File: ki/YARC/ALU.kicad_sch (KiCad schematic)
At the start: 0 parts

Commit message: Major changes to ALU, Flags, and add new ALU controls schematic
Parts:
- added U? (x3): AS6C6264, symbol pdxjjb:AS6C6264
- added U? (x2): 74LS245, symbol 74xx:74LS245
- added U? (x2): 74LS574, symbol 74xx:74LS574
- added U?: 74LS573, symbol 74xx:74LS573
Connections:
- new net A0: U?.10 (A0)
- new net A1: U?.9 (A1)
- new net A2: U?.8 (A2)
- new net A3: U?.7 (A3)
- new net A4: U?.10 (A0), U?.10 (A0)
- new net A5: U?.9 (A1), U?.9 (A1)
- new net A6: U?.8 (A2), U?.8 (A2)
- new net A7: U?.7 (A3), U?.7 (A3)
- new net ALUOUT0: U?.19 (Q0)
- new net ALUOUT15: U?.12 (Q7)
- new net ALUOUT7: U?.12 (Q7)
- new net ALUOUT8: U?.19 (Q0)
- new net ALU_D0: U?.11 (DQ0), U?.2 (A0), U?.2 (D0), U?.2 (D0)
- new net ALU_D1: U?.12 (DQ1), U?.3 (A1)
- new net ALU_D2: U?.13 (DQ2), U?.4 (A2)
- new net ALU_D3: U?.15 (DQ3), U?.5 (A3)
- new net ALU_D4: U?.11 (DQ0), U?.11 (DQ0), U?.2 (A0)
- new net ALU_D5: U?.12 (DQ1), U?.12 (DQ1), U?.3 (A1)
- new net ALU_D6: U?.13 (DQ2), U?.13 (DQ2), U?.4 (A2)
- new net ALU_D7: U?.15 (DQ3), U?.15 (DQ3), U?.5 (A3), U?.9 (D7), U?.9 (D7)
- new net B0: U?.6 (A4)
- new net B1: U?.5 (A5)
- new net B2: U?.4 (A6)
- new net B3: U?.3 (A7)
- new net B4: U?.6 (A4), U?.6 (A4)
- new net B5: U?.5 (A5), U?.5 (A5)
- new net B6: U?.4 (A6), U?.4 (A6)
- new net B7: U?.3 (A7), U?.3 (A7)
- new net CARRY_IN: U?.25 (A8)
- new net DN4: U?.16 (DQ4), U?.6 (A4)
- new net DN5: U?.17 (DQ5), U?.7 (A5)
- new net DN6: U?.18 (DQ6), U?.8 (A6)
- new net DN7: U?.19 (DQ7), U?.9 (A7)
- new net F0: U?.16 (DQ4), U?.16 (DQ4), U?.6 (A4)
- new net F1: U?.17 (DQ5), U?.17 (DQ5), U?.7 (A5)
- new net F2: U?.18 (DQ6), U?.18 (DQ6), U?.8 (A6)
- new net F3: U?.19 (DQ7), U?.19 (DQ7), U?.9 (A7)
- new net FMUX0: U?.2 (D0)
- new net FMUX1: U?.3 (D1)
- new net FMUX2: U?.4 (D2)
- new net FMUX3: U?.5 (D3)
- new net GND: U?.1 (OE), U?.1 (OE), U?.10 (GND), U?.10 (GND), U?.10 (GND), U?.10 (GND), U?.10 (GND), U?.14 (GND), U?.14 (GND), U?.14 (GND), U?.6 (D4), U?.7 (D5), U?.8 (D6), U?.9 (D7)
- new net HALF_CARRY_IN: U?.25 (A8), U?.25 (A8)
- new net IRH0: U?.24 (A9), U?.24 (A9), U?.24 (A9)
- new net IRH1: U?.21 (A10), U?.21 (A10), U?.21 (A10)
- new net IRH2: U?.23 (A11), U?.23 (A11), U?.23 (A11)
- new net IRH3: U?.2 (A12), U?.2 (A12), U?.2 (A12)
- new net KX0: U?.18 (B0), U?.18 (B0)
- new net KX7: U?.11 (B7), U?.11 (B7)
- new net LONG_SYMBOL: U?.1 (OE), U?.11 (Cp), U?.19 (CE), U?.20 (CE#)
- new net REG_F0: U?.19 (Q0)
- new net REG_F1: U?.18 (Q1)
- new net REG_F2: U?.17 (Q2)
- new net REG_F3: U?.16 (Q3)
- new net VCC: U?.20 (VCC), U?.20 (VCC), U?.20 (VCC), U?.20 (VCC), U?.20 (VCC), U?.28 (Vcc), U?.28 (Vcc), U?.28 (Vcc)
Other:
- note added: "C Z N V"
- note added: "HC HZ HN HV"
- note added: "V N Z C"

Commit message: Believable ALU/Flags design almost complete
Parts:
- removed U?: 74LS574, symbol 74xx:74LS574
- gave numbers to parts that had none: 7
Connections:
- net GND: now also U116.20 (CE#), U117.20 (CE#), U117.25 (A8), U118.20 (CE#), U118.22 (OE#); no longer U122.1 (OE)
- net LONG_SYMBOL: no longer U116.20 (CE#)
- net VCC: now also U116.25 (A8), U116.26 (CE2), U117.26 (CE2), U118.26 (CE2)
- net ~{FQTR_NOT_C}: now reaches U117.22 (OE#)
- net ~{ALU_WR}: now reaches U117.27 (WE#)
- net ~{ALU_WR}: now also U116.27 (WE#), U118.27 (WE#)
- net ~{FQTR_C}: now reaches U116.22 (OE#)
- net F0 renamed FHALF.C
- net F1 renamed FHALF.Z
- net F2 renamed FHALF.N
- net F3 renamed FHALF.V
- removed net HALF_CARRY_IN: U116.25 (A8), U117.25 (A8)
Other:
- note added: "FMUXIN_Z SHEET 17"
- note removed: "C Z N V"
- note removed: "HC HZ HN HV"
- note removed: "V N Z C"

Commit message: Further development of ALU controls
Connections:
- net GND: now also U122.1 (OE); no longer U117.25 (A8), U118.22 (OE#)
- net VCC: no longer U116.25 (A8), U116.26 (CE2), U117.26 (CE2)
- net SYSADDR15: now reaches U120.1 (A->B)
- net SYSADDR15: now also U119.1 (A->B)
- net ACR3: now reaches U120.19 (CE)
- net PHI_1_CLK: now reaches U121.11 (Load)
- net LONG_SYMBOL renamed ACR2
- net ACR2: no longer U122.11 (Cp)
- net ~{ALU_WR} renamed ACR7
- new net ACR4: U116.25 (A8)
- new net ACR5: U117.25 (A8)
- new net ACR6: U118.22 (OE#)
- new net PHI_2_CLK: U122.11 (Cp)
- new net ~{ACR_ERR}: U116.26 (CE2), U117.26 (CE2)

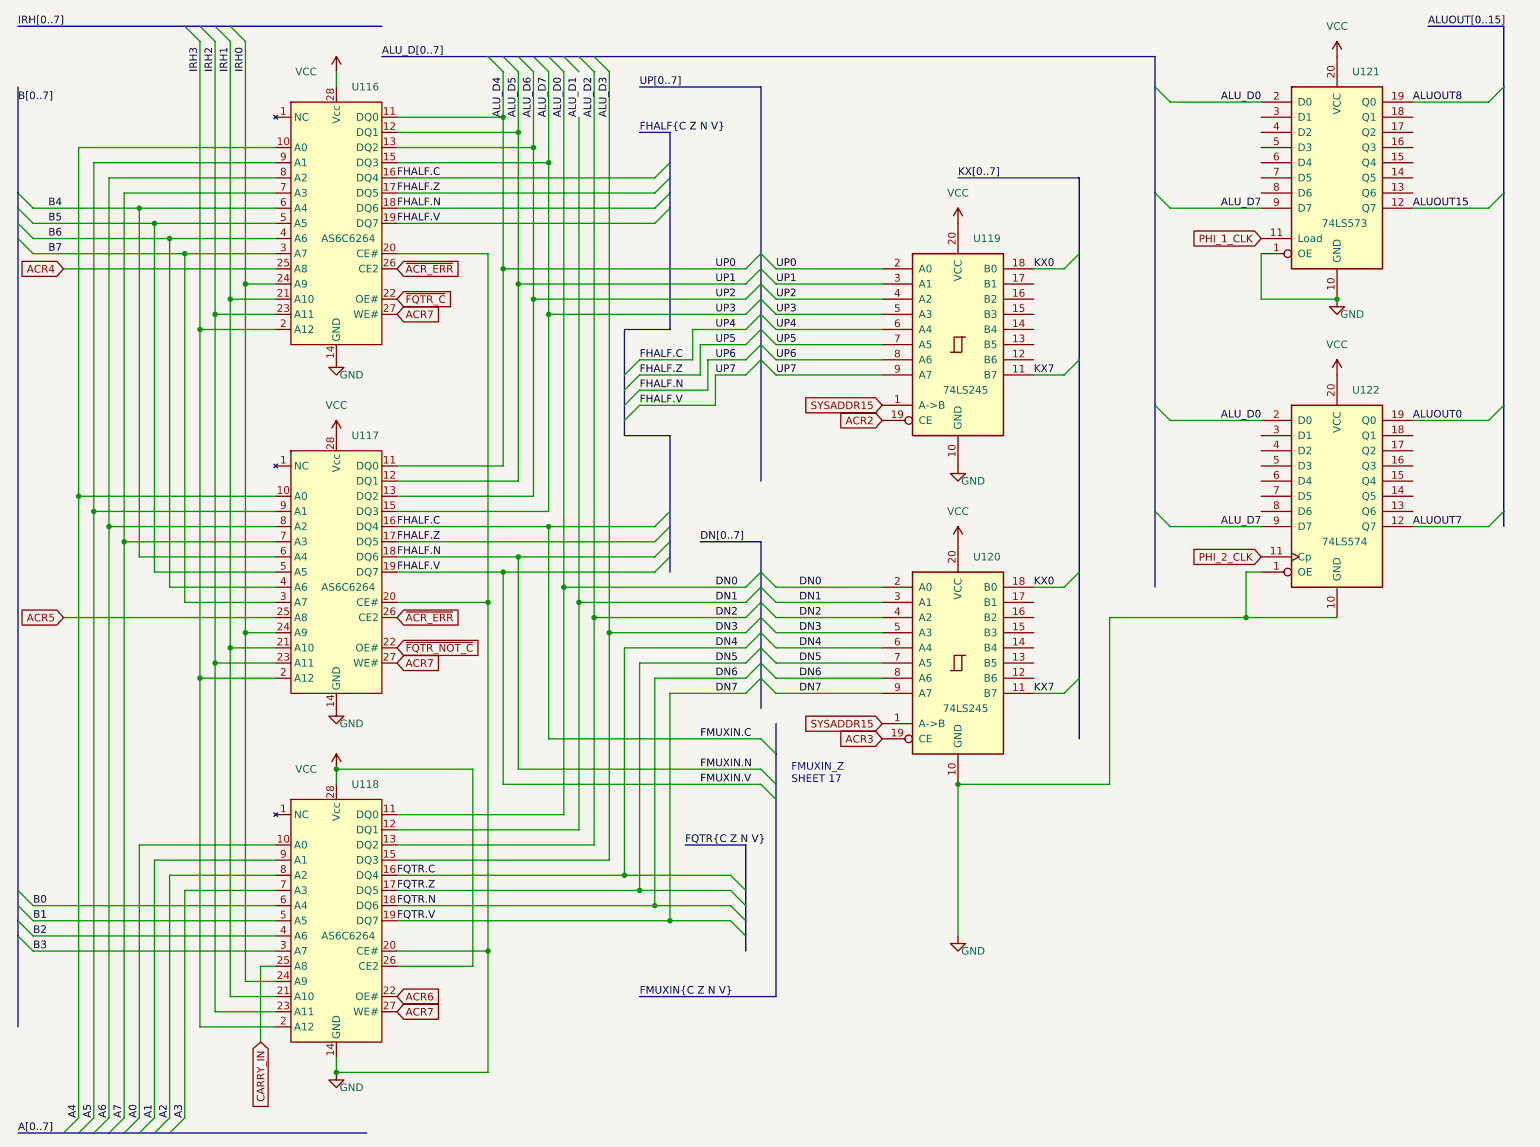
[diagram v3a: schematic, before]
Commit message: ALU schematic checking complete. Ready to start layout.
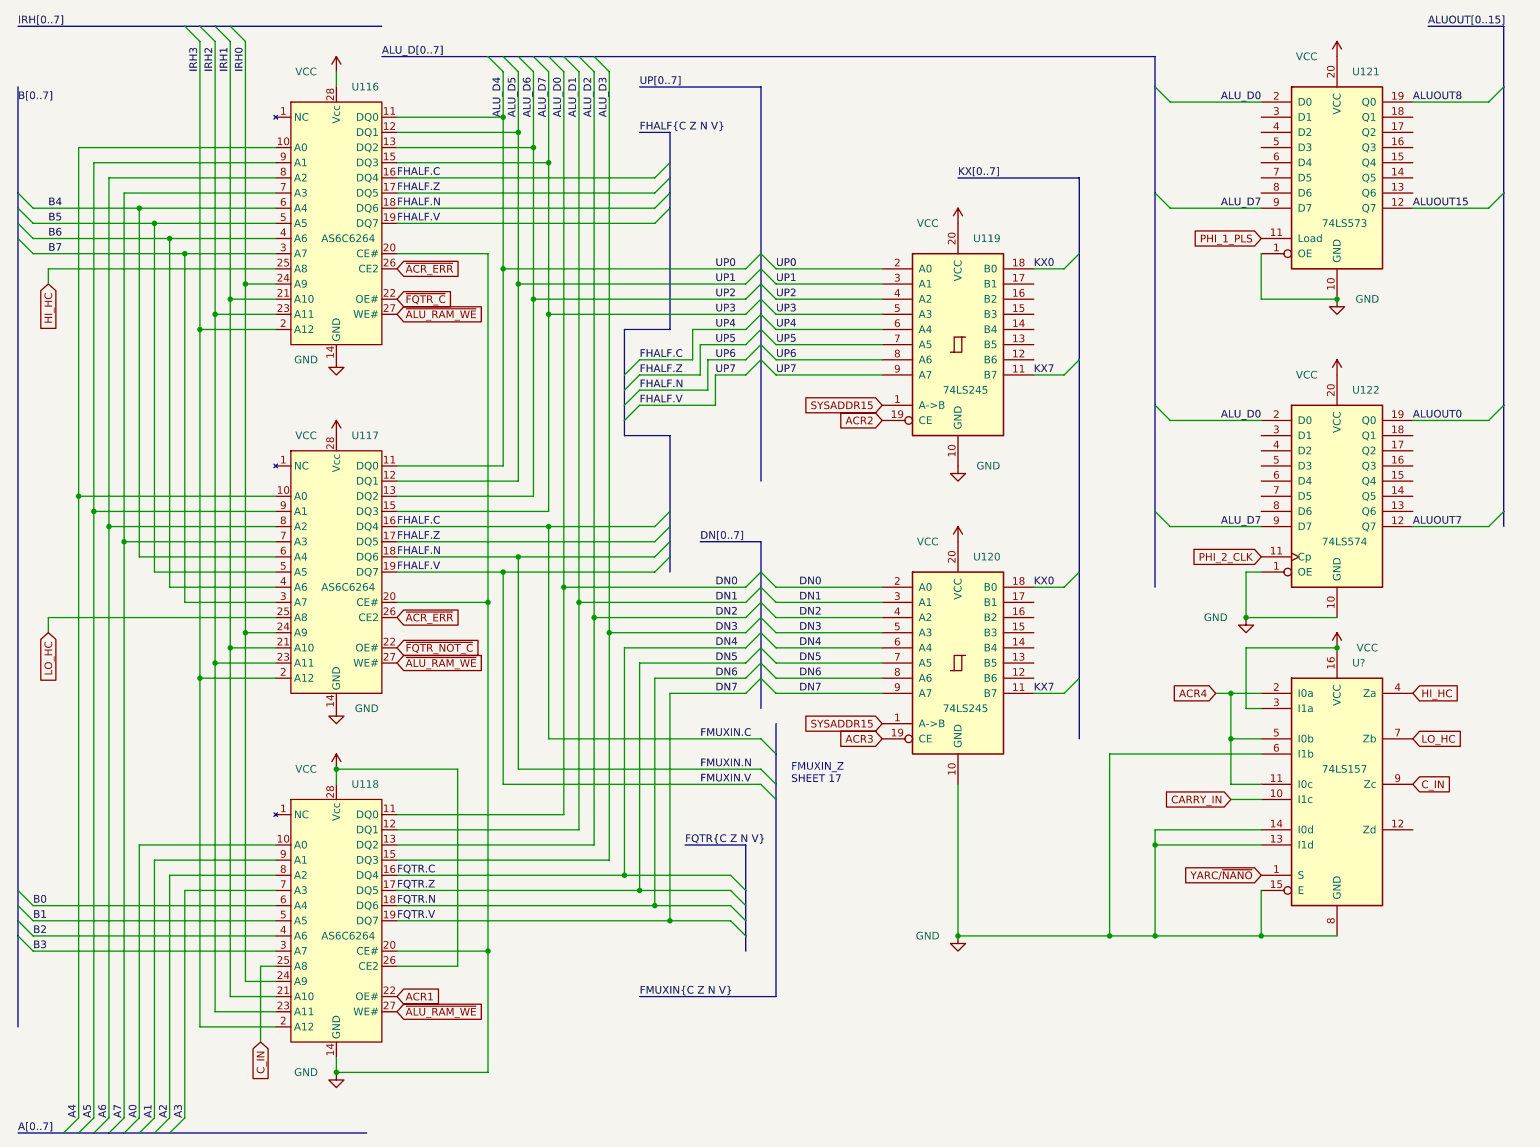
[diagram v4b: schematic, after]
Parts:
- added U?: 74LS157, symbol 74xx:74LS157
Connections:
- net ACR4: now also U?.11 (I0c), U?.2 (I0a), U?.5 (I0b); no longer U116.25 (A8)
- net CARRY_IN: now also U?.10 (I1c); no longer U118.25 (A8)
- net GND: now also U?.13 (I1d), U?.14 (I0d), U?.15 (E), U?.6 (I1b), U?.8 (GND)
- net VCC: now also U?.16 (VCC), U?.3 (I1a)
- net ACR5 renamed LO_HC
- net LO_HC: now also U?.7 (Zb)
- net ACR6 renamed ACR1
- net ACR7 renamed ~{ALU_RAM_WE}
- net PHI_1_CLK renamed PHI_1_PLS
- new net C_IN: U118.25 (A8), U?.9 (Zc)
- new net HI_HC: U116.25 (A8), U?.4 (Za)
- new net YARC/~{NANO}: U?.1 (S)

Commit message: Redesign of ALU control logic
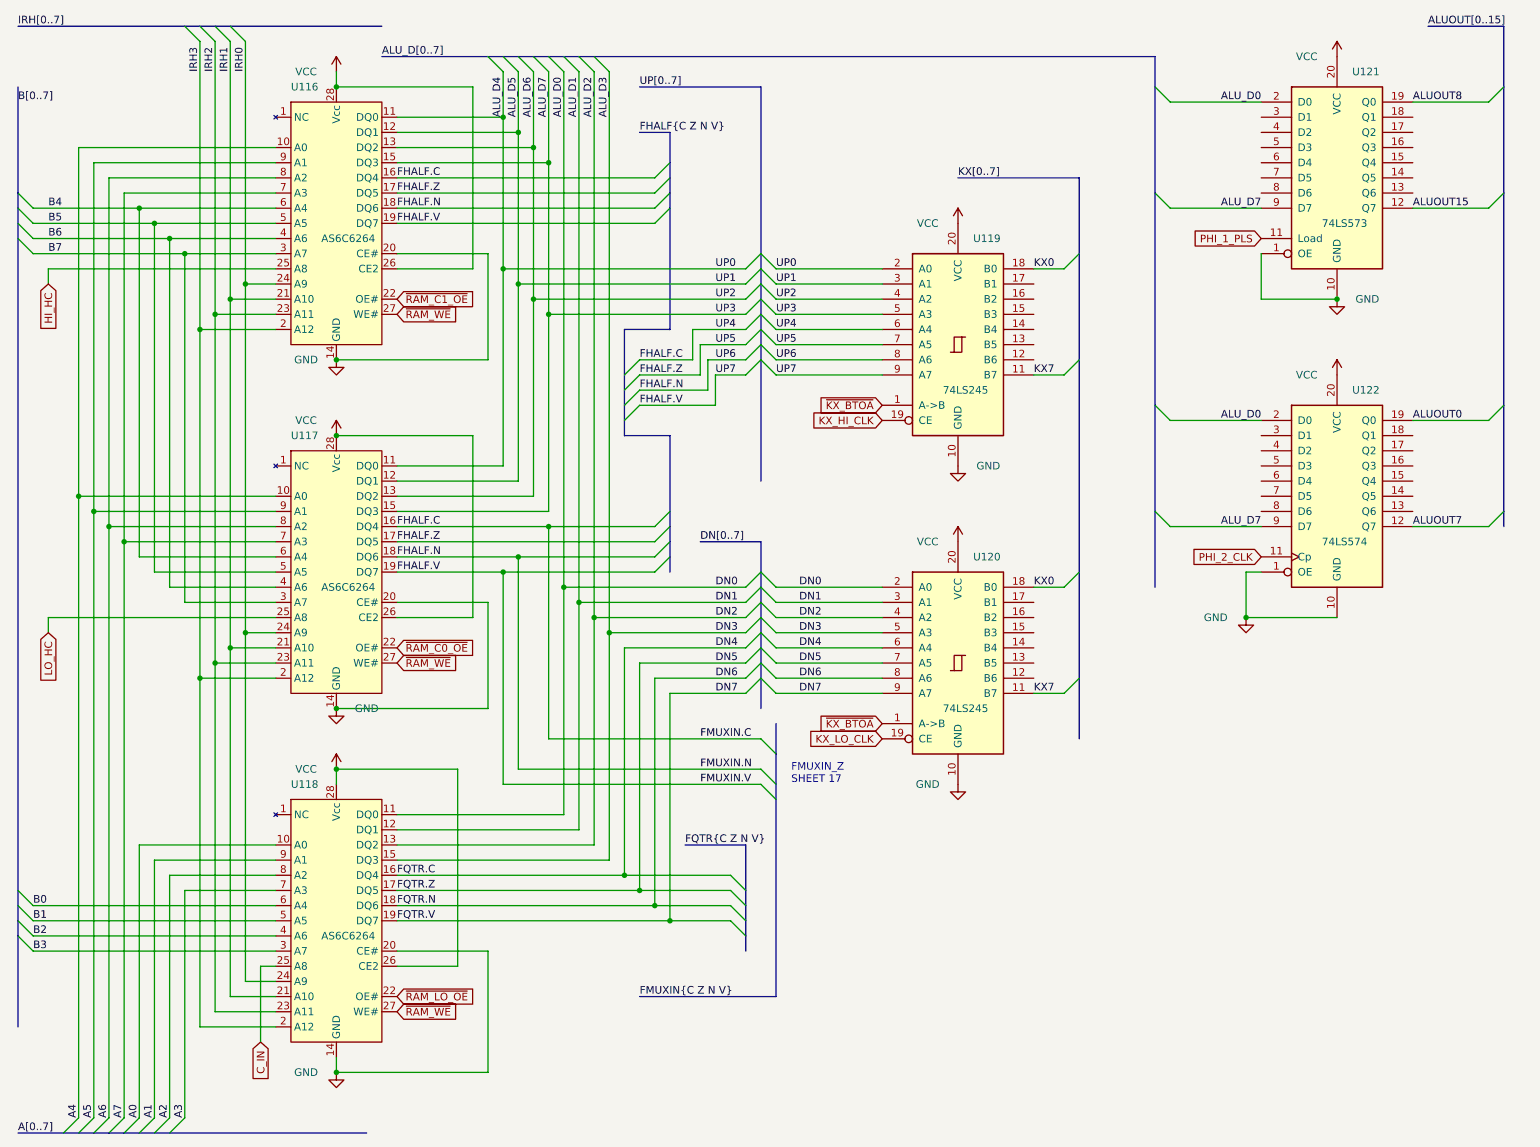
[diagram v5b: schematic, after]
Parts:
- removed U?: 74LS157, symbol 74xx:74LS157
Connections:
- net ~{ACR_ERR} is gone; now on net VCC: U116.26 (CE2), U117.26 (CE2)
- net ACR1 renamed ~{RAM_LO_OE}
- net ACR2 renamed KX_HI_CLK
- net ACR3 renamed KX_LO_CLK
- net SYSADDR15 renamed ~{KX_BTOA}
- net ~{ALU_RAM_WE} renamed ~{RAM_WE}
- net ~{FQTR_C} renamed ~{RAM_C1_OE}
- net ~{FQTR_NOT_C} renamed ~{RAM_C0_OE}

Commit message: Yet more cleanup on ALU and flags design
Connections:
- net PHI_1_PLS renamed PHI_2_PLS
- net PHI_2_CLK renamed PHI_1_CLK
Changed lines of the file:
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@@
     (effects (font (size 1.27 1.27)) (justify left bottom))
   )
-  (global_label "PHI_1_PLS" (shape input) (at 223.52 50.8 180) (fields_autoplaced)
+  (global_label "PHI_2_PLS" (shape input) (at 223.52 50.8 180) (fields_autoplaced)
     (effects (font (size 1.27 1.27)) (justify right))
     (property "Intersheet References" "${INTERSHEET_REFS}" (id 0) (at 211.2493 50.7206 0)
@@
     )
   )
-  (global_label "PHI_2_CLK" (shape input) (at 223.52 104.14 180) (fields_autoplaced)
+  (global_label "PHI_1_CLK" (shape input) (at 223.52 104.14 180) (fields_autoplaced)
     (effects (font (size 1.27 1.27)) (justify right))
-    (property "Intersheet References" "${INTERSHEET_REFS}" (id 0) (at 211.1888 104.2194 0)
+    (property "Intersheet References" "${INTERSHEET_REFS}" (id 0) (at 211.1888 104.0606 0)
       (effects (font (size 1.27 1.27)) (justify right) hide)
     )

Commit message: Ongoing corrections and improvements
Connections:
- net ALUOUT0: now also U122.12 (Q7); no longer U122.19 (Q0)
- net ALUOUT15: now also U121.19 (Q0); no longer U121.12 (Q7)
- net ALUOUT7: now also U122.19 (Q0); no longer U122.12 (Q7)
- net ALUOUT8: now also U121.12 (Q7); no longer U121.19 (Q0)
- net ALU_D0: now also U121.9 (D7), U122.9 (D7); no longer U121.2 (D0), U122.2 (D0)
- net ALU_D7: now also U121.2 (D0), U122.2 (D0); no longer U121.9 (D7), U122.9 (D7)
- net KX_HI_CLK renamed ~{KX_HI_OE}
- net KX_LO_CLK renamed ~{KX_LO_OE}

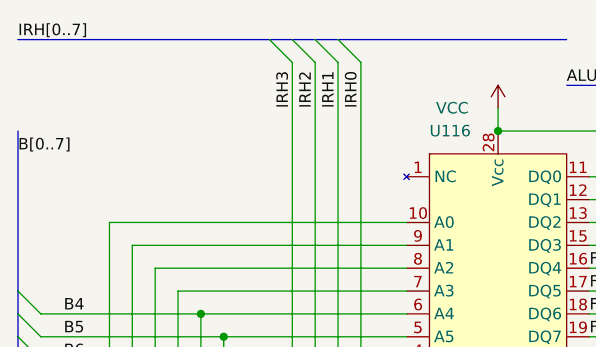
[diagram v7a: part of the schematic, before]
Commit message: Add the ACN mini-bus which can come from the instruction bits 11:8 or from the microcode bits 23:20. It selects the ALU operation and the condition codes.
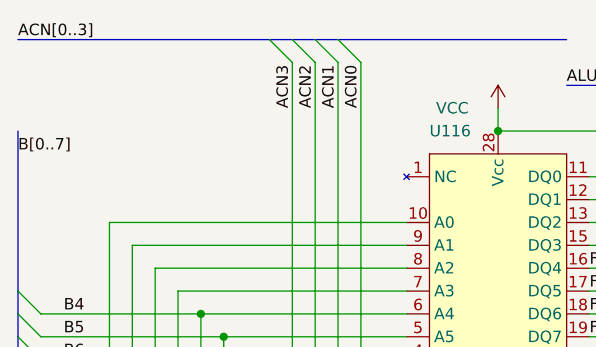
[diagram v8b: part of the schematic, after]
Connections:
- net IRH0 renamed ACN0
- net IRH1 renamed ACN1
- net IRH2 renamed ACN2
- net IRH3 renamed ACN3
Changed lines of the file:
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@@
-    (effects (font (size 1.27 1.27)) (justify left bottom))
-  )
-  (label "IRH0" (at 53.34 22.86 90)
     (effects (font (size 1.27 1.27)) (justify left bottom))
   )
@@
     (effects (font (size 1.27 1.27)) (justify left bottom))
   )
+  (label "ACN3" (at 45.72 22.86 90)
+    (effects (font (size 1.27 1.27)) (justify left bottom))
+  )
   (label "A0" (at 35.56 198.12 90)
     (effects (font (size 1.27 1.27)) (justify left bottom))
@@
     (effects (font (size 1.27 1.27)) (justify left bottom))
   )
-  (label "IRH3" (at 45.72 22.86 90)
-    (effects (font (size 1.27 1.27)) (justify left bottom))
-  )
   (label "ALU_D3" (at 114.3 30.48 90)
     (effects (font (size 1.27 1.27)) (justify left bottom))
   )
-  (label "IRH1" (at 50.8 22.86 90)
+  (label "ACN2" (at 48.26 22.86 90)
     (effects (font (size 1.27 1.27)) (justify left bottom))
   )
@@
     (effects (font (size 1.27 1.27)) (justify left bottom))
   )
+  (label "ACN0" (at 53.34 22.86 90)
+    (effects (font (size 1.27 1.27)) (justify left bottom))
+  )
   (label "DN0" (at 149.86 109.22 180)
     (effects (font (size 1.27 1.27)) (justify right bottom))
@@
     (effects (font (size 1.27 1.27)) (justify left bottom))
   )
-  (label "IRH[0..7]" (at 15.24 15.24 0)
+  (label "ACN[0..3]" (at 15.24 15.24 0)
     (effects (font (size 1.27 1.27)) (justify left bottom))
   )
@@
     (effects (font (size 1.27 1.27)) (justify left bottom))
   )
-  (label "IRH2" (at 48.26 22.86 90)
-    (effects (font (size 1.27 1.27)) (justify left bottom))
-  )
   (label "DN5" (at 149.86 121.92 180)
     (effects (font (size 1.27 1.27)) (justify right bottom))
@@
     (effects (font (size 1.27 1.27)) (justify left bottom))
   )
+  (label "ACN1" (at 50.8 22.86 90)
+    (effects (font (size 1.27 1.27)) (justify left bottom))
+  )
